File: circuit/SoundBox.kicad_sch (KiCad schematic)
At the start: 1 part, among them U1 RP2040

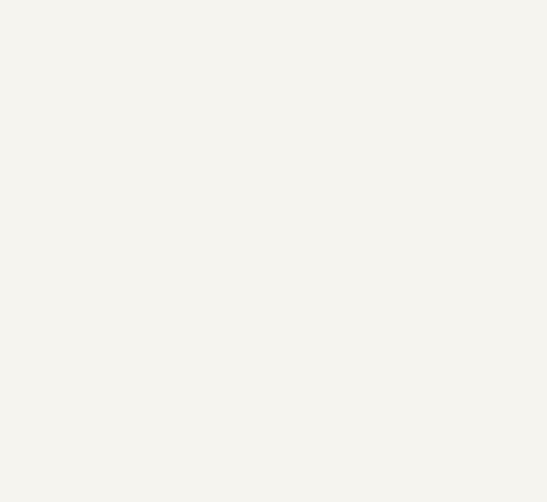
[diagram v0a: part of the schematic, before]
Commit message: Move to Arduino / PlatformIO
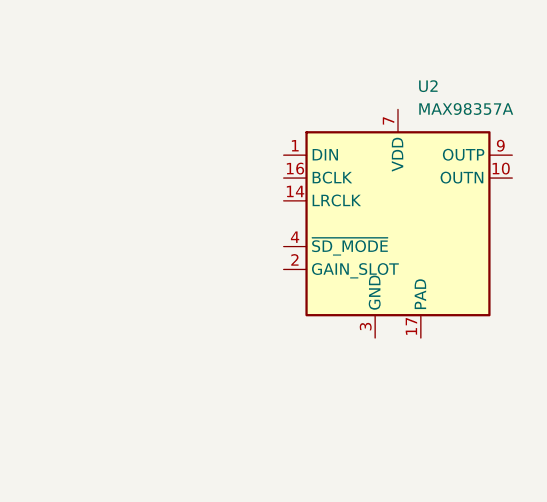
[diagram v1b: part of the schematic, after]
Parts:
- added U2: MAX98357A, Package_DFN_QFN:TQFN-16-1EP_3x3mm_P0.5mm_EP1.23x1.23mm, symbol Audio:MAX98357A
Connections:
- new net: U2.11 (GND), U2.15 (GND), U2.3 (GND)
- new net: U2.7 (VDD), U2.8 (VDD)
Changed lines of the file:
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@@
 	(paper "A4")
+	(symbol
+		(lib_id "Audio:MAX98357A")
+		(at 149.86 72.39 0)
+		(unit 1)
+		(exclude_from_sim no)
+		(in_bom yes)
+		(on_board yes)
+		(dnp no)
+		(fields_autoplaced yes)
+		(property "Reference" "U2"
+			(at 152.0541 57.15 0)
+			(effects
+				(font
+					(size 1.27 1.27)
+				)
+				(justify left)
+			)
+		)
+		(property "Value" "MAX98357A"
+			(at 152.0541 59.69 0)
+			(effects
+				(font
+					(size 1.27 1.27)
+				)
+				(justify left)
+			)
+		)
+		(property "Footprint" "Package_DFN_QFN:TQFN-16-1EP_3x3mm_P0.5mm_EP1.23x1.23mm"
+			(at 148.59 74.93 0)
+			(effects
+				(font
+					(size 1.27 1.27)
+				)
+				(hide yes)
+			)
+		)
+		(property "Datasheet" "https://www.analog.com/media/en/technical-documentation/data-sheets/MAX98357A-MAX98357B.pdf"
+			(at 149.86 74.93 0)
+			(effects
+				(font
+					(size 1.27 1.27)
+				)
+				(hide yes)
+			)
+		)
+		(property "Description" "Mono DAC with amplifier, I2S, PCM, TDM, 32-bit, 96khz, 3.2W, TQFP-16"
+			(at 149.86 72.39 0)
+			(effects
+				(font
+					(size 1.27 1.27)
+				)
+				(hide yes)
+			)
+		)
+		(pin "3"
+		)
+		(pin "4"
+		)
+		(pin "5"
+		)
+		(pin "6"
+		)
+		(pin "1"
+		)
+		(pin "10"
+		)
+		(pin "16"
+		)
+		(pin "17"
+		)
+		(pin "2"
+		)
+		(pin "11"
+		)
+		(pin "12"
+		)
+		(pin "13"
+		)
+		(pin "14"
+		)
+		(pin "15"
+		)
+		(pin "7"
+		)
+		(pin "8"
+		)
+		(pin "9"
+		)
+		(instances
+			(project "SoundBox"
+				(path "/00799033-309c-413a-90af-bec8af2d644c"
+					(reference "U2")
+					(unit 1)
+				)
+			)
+		)
+	)
 	(symbol
 		(lib_id "MCU_RaspberryPi:RP2040")
